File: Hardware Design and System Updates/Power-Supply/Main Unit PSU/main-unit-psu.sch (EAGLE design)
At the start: 18 parts, among them U1 BA033CC0FP-E2TO252-3_ROM, U2 BA033CC0FP-E2TO252-3_ROM, U3 L7805CV

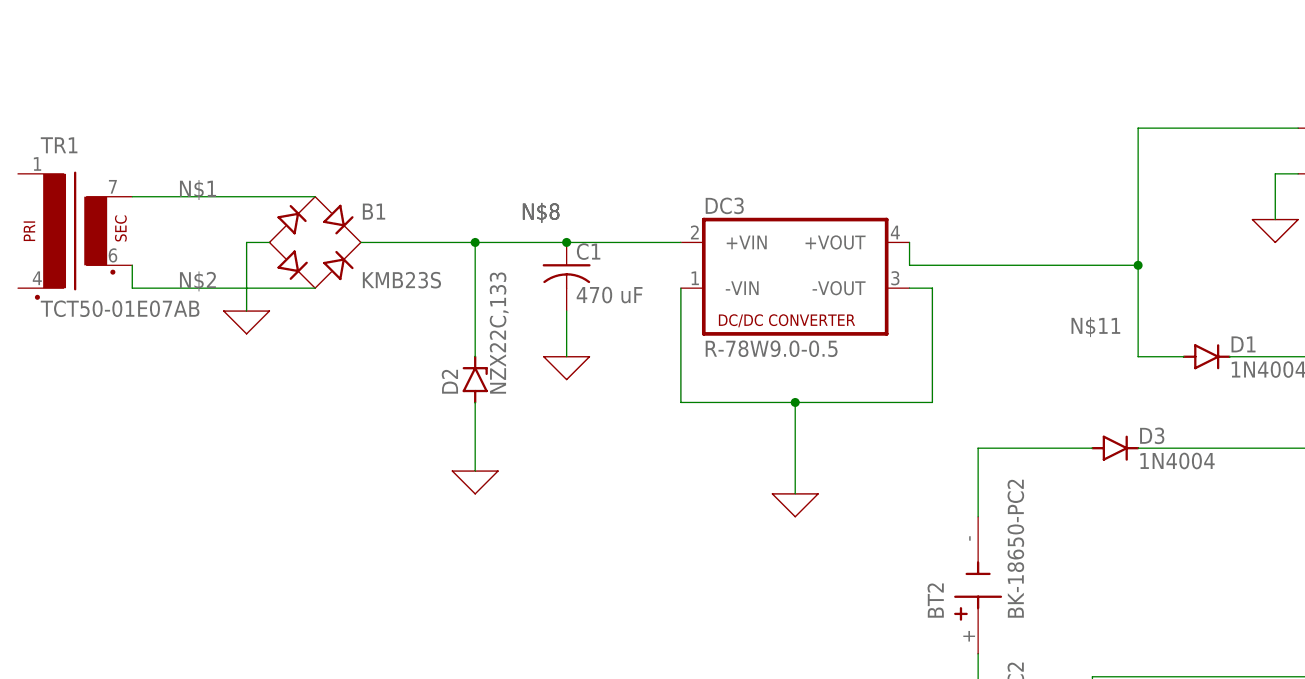
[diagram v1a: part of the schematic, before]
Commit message: Fixed system schematics
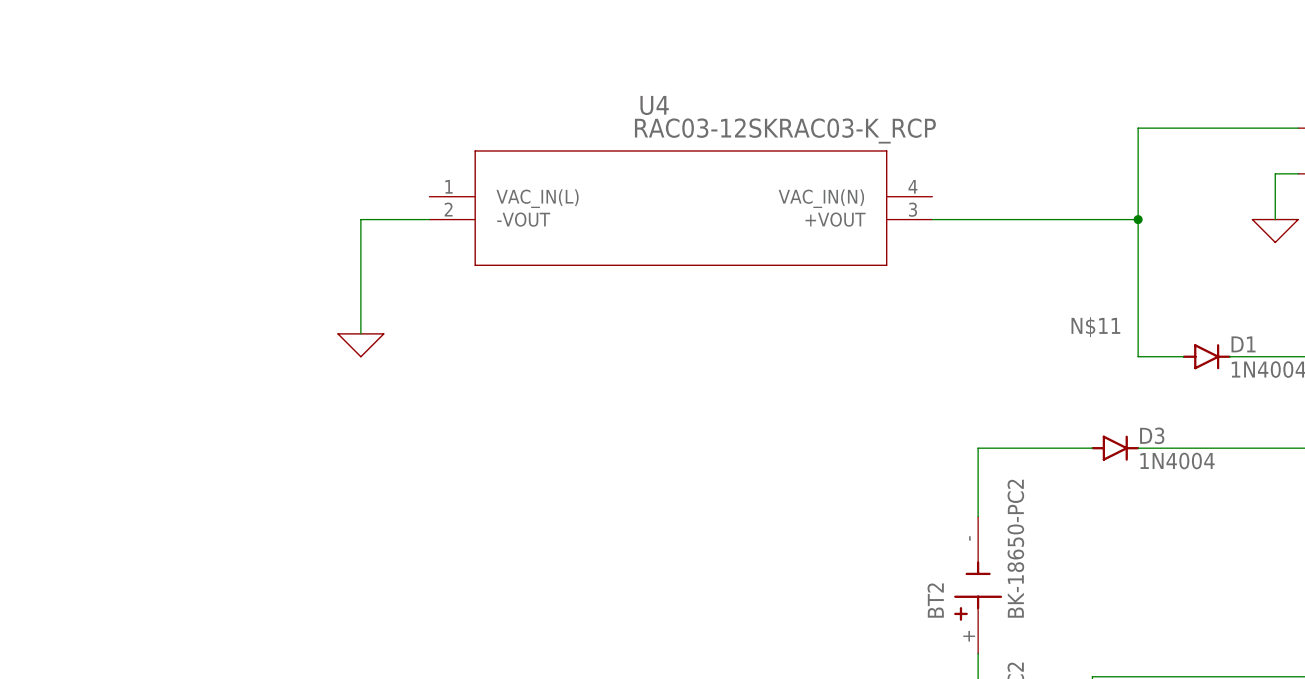
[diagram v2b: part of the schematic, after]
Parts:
- removed B1: KMB23S, rectifier:B-DIL
- removed C1: 470 uF, rcl:C-US050-024X044
- removed D2: NZX22C,133, diode:ZENER-DIODEDO41Z10
- removed DC3: R-78W9.0-0.5, dc-dc-converter:NME
- removed TR1: TCT50-01E07AB, trafo:EE20-1
- added U4: RAC03-12SKRAC03-K_RCP, 2023-04-05_11-47-46_Library:RAC03-12SKRAC03-K_RCP
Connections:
- removed net N$1: B1.AC1, TR1.S4
- removed net N$2: B1.AC2, TR1.S3
- removed net N$8: B1.+, C1.1, D2.C, DC3.+VIN
- net 0: now also U4.-VOUT; no longer B1.-, C1.2, D2.A, DC3.-VIN, DC3.-VOUT
- net N$11: now also U4.+VOUT; no longer DC3.+VOUT
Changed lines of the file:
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@@
 <parts>
 <part name="D1" library="diode" library_urn="urn:adsk.eagle:library:210" deviceset="1N4004" device="" package3d_urn="urn:adsk.eagle:package:43336/1"/>
-<part name="C1" library="rcl" library_urn="urn:adsk.eagle:library:334" deviceset="C-US" device="050-024X044" package3d_urn="urn:adsk.eagle:package:23643/1" value="470 uF"/>
-<part name="B1" library="rectifier" library_urn="urn:adsk.eagle:library:336" deviceset="B-DIL" device="" package3d_urn="urn:adsk.eagle:package:23868/1" value="KMB23S"/>
-<part name="X_1" library="ngspice-simulation" library_urn="urn:adsk.eagle:library:527439" deviceset="GND" device=""/>
-<part name="D2" library="diode" library_urn="urn:adsk.eagle:library:210" deviceset="ZENER-DIODE" device="DO41Z10" package3d_urn="urn:adsk.eagle:package:43341/1" value="NZX22C,133"/>
-<part name="X_2" library="ngspice-simulation" library_urn="urn:adsk.eagle:library:527439" deviceset="GND" device=""/>
-<part name="X_3" library="ngspice-simulation" library_urn="urn:adsk.eagle:library:527439" deviceset="GND" device=""/>
-<part name="TR1" library="trafo" library_urn="urn:adsk.eagle:library:394" deviceset="EE20-1" device="" package3d_urn="urn:adsk.eagle:package:28342/1" value="TCT50-01E07AB"/>
 <part name="DC1" library="dc-dc-converter" library_urn="urn:adsk.eagle:library:208" deviceset="NME" device="" package3d_urn="urn:adsk.eagle:package:12313/1" value="K7803-500R3"/>
 <part name="X_4" library="ngspice-simulation" library_urn="urn:adsk.eagle:library:527439" deviceset="GND" device=""/>
@@
 <part name="BT1" library="BK-18650-PC2" deviceset="BK-18650-PC2" device=""/>
 <part name="X_5" library="ngspice-simulation" library_urn="urn:adsk.eagle:library:527439" deviceset="GND" device=""/>
-<part name="DC3" library="dc-dc-converter" library_urn="urn:adsk.eagle:library:208" deviceset="NME" device="" package3d_urn="urn:adsk.eagle:package:12313/1" value="R-78W9.0-0.5"/>
-<part name="X_7" library="ngspice-simulation" library_urn="urn:adsk.eagle:library:527439" deviceset="GND" device=""/>
 <part name="U1" library="2023-03-08_12-17-23_Library" deviceset="BA033CC0FP-E2" device="TO252-3_ROM"/>
 <part name="X_8" library="ngspice-simulation" library_urn="urn:adsk.eagle:library:527439" deviceset="GND" device=""/>
@@
 <part name="C4" library="rcl" library_urn="urn:adsk.eagle:library:334" deviceset="C-US" device="050-024X044" package3d_urn="urn:adsk.eagle:package:23643/1" value="0.1 uF"/>
 <part name="X_14" library="ngspice-simulation" library_urn="urn:adsk.eagle:library:527439" deviceset="GND" device=""/>
+<part name="U4" library="2023-04-05_11-47-46_Library" deviceset="RAC03-12SK" device="RAC03-K_RCP"/>
+<part name="X_1" library="ngspice-simulation" library_urn="urn:adsk.eagle:library:527439" deviceset="GND" device=""/>
 </parts>
 <sheets>
@@
 <attribute name="VALUE" x="78.74" y="53.5686" size="1.778" layer="96"/>
 </instance>
-<instance part="C1" gate="G$1" x="5.08" y="66.04" smashed="yes">
-<attribute name="NAME" x="6.096" y="66.675" size="1.778" layer="95"/>
-<attribute name="VALUE" x="6.096" y="61.849" size="1.778" layer="96"/>
-</instance>
-<instance part="B1" gate="1" x="-22.86" y="68.58" smashed="yes">
-<attribute name="VALUE" x="-17.78" y="63.5" size="1.778" layer="96"/>
-<attribute name="NAME" x="-17.78" y="71.12" size="1.778" layer="95"/>
-</instance>
-<instance part="X_1" gate="G$1" x="-30.48" y="60.96" smashed="yes"/>
-<instance part="D2" gate="G$1" x="-5.08" y="53.34" smashed="yes" rot="R90">
-<attribute name="NAME" x="-6.985" y="51.562" size="1.778" layer="95" rot="R90"/>
-<attribute name="VALUE" x="-1.651" y="51.562" size="1.778" layer="96" rot="R90"/>
-</instance>
-<instance part="X_2" gate="G$1" x="-5.08" y="43.18" smashed="yes"/>
-<instance part="X_3" gate="G$1" x="5.08" y="55.88" smashed="yes"/>
-<instance part="TR1" gate="1" x="-50.8" y="71.12" smashed="yes">
-<attribute name="NAME" x="-53.34" y="78.486" size="1.778" layer="95"/>
-<attribute name="VALUE" x="-53.34" y="60.325" size="1.778" layer="96"/>
-</instance>
 <instance part="DC1" gate="G$1" x="124.46" y="53.34" smashed="yes">
 <attribute name="NAME" x="114.3" y="59.055" size="1.778" layer="95"/>
@@
 </instance>
 <instance part="X_5" gate="G$1" x="50.8" y="0" smashed="yes"/>
-<instance part="DC3" gate="G$1" x="30.48" y="66.04" smashed="yes">
-<attribute name="NAME" x="20.32" y="71.755" size="1.778" layer="95"/>
-<attribute name="VALUE" x="20.32" y="55.88" size="1.778" layer="96"/>
-</instance>
-<instance part="X_7" gate="G$1" x="30.48" y="40.64" smashed="yes"/>
 <instance part="U1" gate="A" x="147.32" y="55.88" smashed="yes">
 <attribute name="NAME" x="165.4546" y="64.9986" size="2.083" layer="95" ratio="6"/>
@@
 </instance>
 <instance part="X_14" gate="G$1" x="165.1" y="0" smashed="yes"/>
+<instance part="U4" gate="A" x="-12.7" y="73.66" smashed="yes">
+<attribute name="NAME" x="13.0546" y="82.7786" size="2.083" layer="95" ratio="6"/>
+<attribute name="VALUE" x="12.4152" y="80.2386" size="2.083" layer="96" ratio="6"/>
+</instance>
+<instance part="X_1" gate="G$1" x="-17.78" y="58.42" smashed="yes"/>
 </instances>
 <busses>
@@
 <net name="0" class="0">
 <segment>
-<pinref part="D2" gate="G$1" pin="A"/>
-<pinref part="X_2" gate="G$1" pin="0"/>
-<wire x1="-5.08" y1="50.8" x2="-5.08" y2="43.18" width="0.1524" layer="91"/>
-</segment>
-<segment>
-<pinref part="C1" gate="G$1" pin="2"/>
-<pinref part="X_3" gate="G$1" pin="0"/>
-<wire x1="5.08" y1="60.96" x2="5.08" y2="55.88" width="0.1524" layer="91"/>
-</segment>
-<segment>
 <pinref part="X_4" gate="G$1" pin="0"/>
 <pinref part="DC1" gate="G$1" pin="-VIN"/>
@@
 </segment>
 <segment>
-<pinref part="X_1" gate="G$1" pin="0"/>
-<wire x1="-30.48" y1="60.96" x2="-30.48" y2="68.58" width="0.1524" layer="91"/>
-<pinref part="B1" gate="1" pin="-"/>
-<wire x1="-30.48" y1="68.58" x2="-27.94" y2="68.58" width="0.1524" layer="91"/>
-</segment>
-<segment>
 <pinref part="X_5" gate="G$1" pin="0"/>
 <pinref part="BT1" gate="G$1" pin="+"/>
 <wire x1="50.8" y1="0" x2="50.8" y2="2.54" width="0.1524" layer="91"/>
-</segment>
-<segment>
-<pinref part="DC3" gate="G$1" pin="-VIN"/>
-<wire x1="17.78" y1="63.5" x2="17.78" y2="50.8" width="0.1524" layer="91"/>
-<wire x1="17.78" y1="50.8" x2="30.48" y2="50.8" width="0.1524" layer="91"/>
-<pinref part="DC3" gate="G$1" pin="-VOUT"/>
-<wire x1="30.48" y1="50.8" x2="45.72" y2="50.8" width="0.1524" layer="91"/>
-<wire x1="45.72" y1="50.8" x2="45.72" y2="63.5" width="0.1524" layer="91"/>
-<wire x1="45.72" y1="63.5" x2="43.18" y2="63.5" width="0.1524" layer="91"/>
-<pinref part="X_7" gate="G$1" pin="0"/>
-<wire x1="30.48" y1="40.64" x2="30.48" y2="50.8" width="0.1524" layer="91"/>
-<junction x="30.48" y="50.8"/>
 </segment>
 <segment>
@@
 <wire x1="165.1" y1="0" x2="165.1" y2="2.54" width="0.1524" layer="91"/>
 </segment>
-</net>
-<net name="N$1" class="0">
-<segment>
-<pinref part="TR1" gate="1" pin="S4"/>
-<pinref part="B1" gate="1" pin="AC1"/>
-<wire x1="-43.18" y1="73.66" x2="-22.86" y2="73.66" width="0.1524" layer="91"/>
-<label x="-38.1" y="73.66" size="1.778" layer="95"/>
-</segment>
-</net>
-<net name="N$2" class="0">
-<segment>
-<pinref part="TR1" gate="1" pin="S3"/>
-<wire x1="-43.18" y1="66.04" x2="-43.18" y2="63.5" width="0.1524" layer="91"/>
-<pinref part="B1" gate="1" pin="AC2"/>
-<wire x1="-43.18" y1="63.5" x2="-22.86" y2="63.5" width="0.1524" layer="91"/>
-<label x="-38.1" y="63.5" size="1.778" layer="95"/>
+<segment>
+<pinref part="X_1" gate="G$1" pin="0"/>
+<wire x1="-17.78" y1="58.42" x2="-17.78" y2="71.12" width="0.1524" layer="91"/>
+<pinref part="U4" gate="A" pin="-VOUT"/>
+<wire x1="-17.78" y1="71.12" x2="-10.16" y2="71.12" width="0.1524" layer="91"/>
 </segment>
 </net>
@@
 </segment>
 </net>
-<net name="N$8" class="0">
-<segment>
-<pinref part="C1" gate="G$1" pin="1"/>
-<pinref part="B1" gate="1" pin="+"/>
-<wire x1="-17.78" y1="68.58" x2="-5.08" y2="68.58" width="0.1524" layer="91"/>
-<pinref part="D2" gate="G$1" pin="C"/>
-<wire x1="-5.08" y1="68.58" x2="5.08" y2="68.58" width="0.1524" layer="91"/>
-<wire x1="-5.08" y1="55.88" x2="-5.08" y2="68.58" width="0.1524" layer="91"/>
-<junction x="-5.08" y="68.58"/>
-<label x="0" y="71.12" size="1.778" layer="95"/>
-<label x="0" y="71.12" size="1.778" layer="95"/>
-<pinref part="DC3" gate="G$1" pin="+VIN"/>
-<wire x1="5.08" y1="68.58" x2="17.78" y2="68.58" width="0.1524" layer="91"/>
-<junction x="5.08" y="68.58"/>
-</segment>
-</net>
 <net name="N$11" class="0">
 <segment>
@@
 <wire x1="68.58" y1="55.88" x2="73.66" y2="55.88" width="0.1524" layer="91"/>
 <wire x1="68.58" y1="81.28" x2="86.36" y2="81.28" width="0.1524" layer="91"/>
-<wire x1="68.58" y1="55.88" x2="68.58" y2="66.04" width="0.1524" layer="91"/>
 <label x="60.96" y="58.42" size="1.778" layer="95"/>
-<pinref part="DC3" gate="G$1" pin="+VOUT"/>
-<wire x1="68.58" y1="66.04" x2="68.58" y2="81.28" width="0.1524" layer="91"/>
-<wire x1="43.18" y1="68.58" x2="43.18" y2="66.04" width="0.1524" layer="91"/>
-<wire x1="43.18" y1="66.04" x2="68.58" y2="66.04" width="0.1524" layer="91"/>
-<junction x="68.58" y="66.04"/>
-</segment>
-</net>
+<wire x1="68.58" y1="55.88" x2="68.58" y2="71.12" width="0.1524" layer="91"/>
+<pinref part="U4" gate="A" pin="+VOUT"/>
+<wire x1="68.58" y1="71.12" x2="68.58" y2="81.28" width="0.1524" layer="91"/>
+<wire x1="45.72" y1="71.12" x2="68.58" y2="71.12" width="0.1524" layer="91"/>
+<junction x="68.58" y="71.12"/>
+</segment>
+</net>
